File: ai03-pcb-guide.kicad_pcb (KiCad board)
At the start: 2 copper layers, 82.5 x 38.1 mm, 24 parts, among them SW1 SW_Push, U1 ATmega32U4-A, Y1 16Mhz

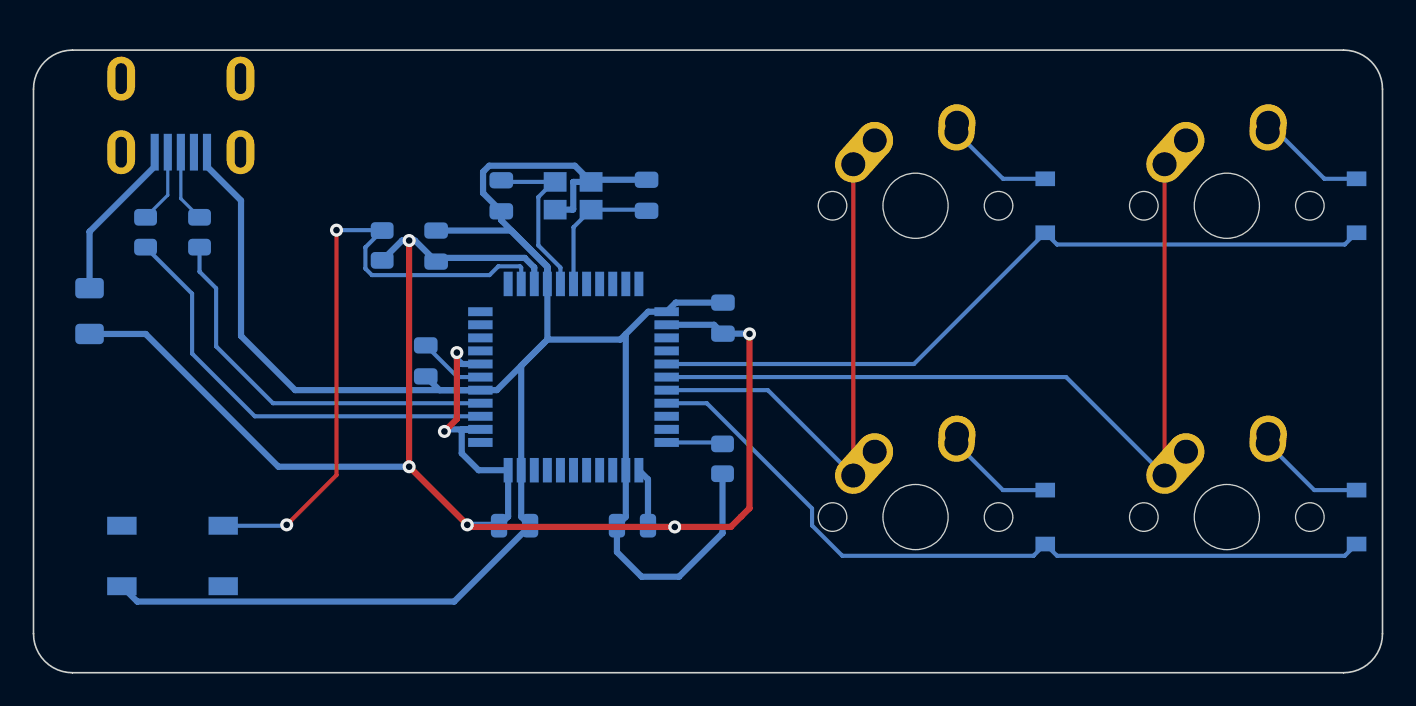
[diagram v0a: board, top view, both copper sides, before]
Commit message: Reroute PCB and add ground fill.
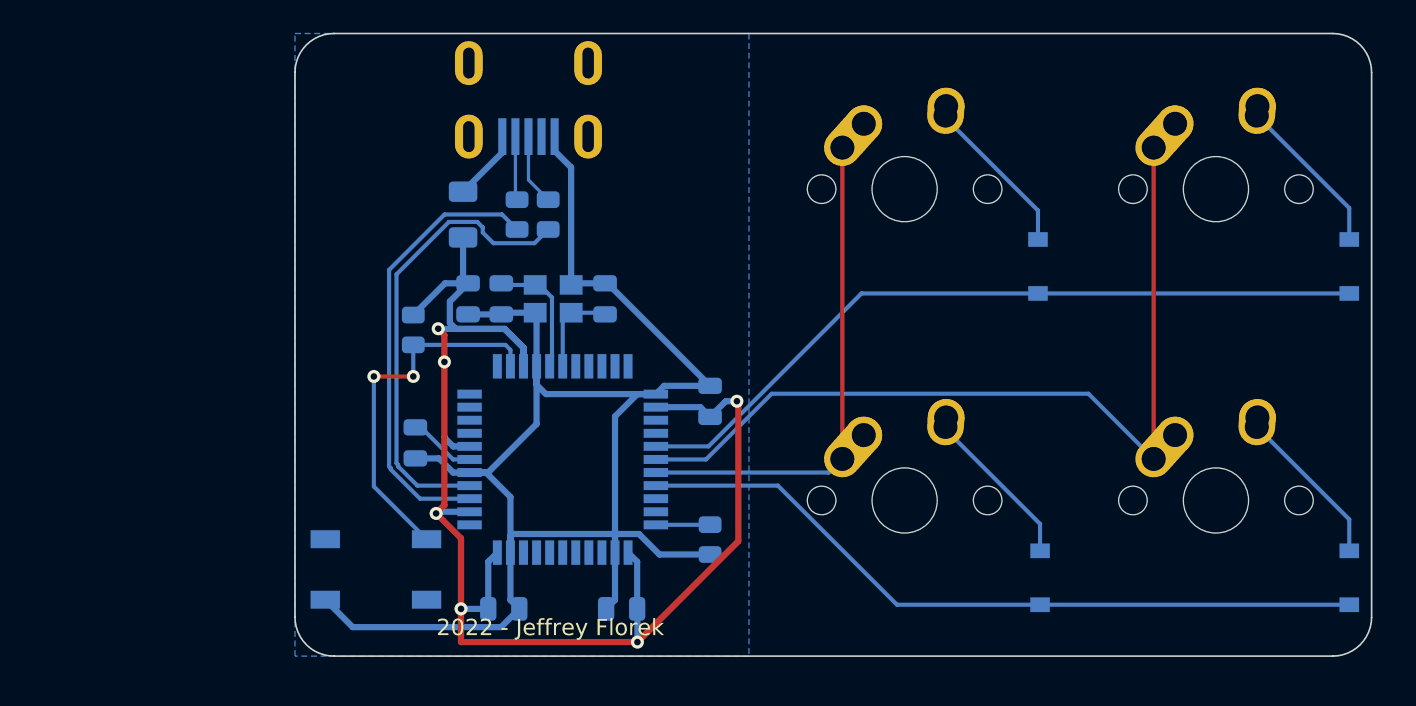
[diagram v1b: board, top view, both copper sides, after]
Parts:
- moved F1 23.6 mm to (118.2, 99.2)
- moved R3 22.8 mm to (121.5, 99.2)
- moved R2 21.4 mm to (123.4, 99.2)
- moved USB1 21.3 mm to (122.2, 89.9)
- moved SW1 12.5 mm to (112.9, 120.9)
- moved C1 6.83 mm to (126.9, 104.3)
- moved Y1 6.42 mm to (123.7, 104.3)
- moved C2 6.31 mm to (120.6, 104.3)
- moved R1 5.51 mm to (115.2, 106.2), turned to -90 degrees
- moved C5 5.15 mm to (133.3, 110.6)
- moved C6 5.14 mm to (127.9, 123.3)
- moved C7 5.14 mm to (120.7, 123.3)
- moved U1 5.08 mm to (124.3, 114.2)
- moved C3 5.06 mm to (115.3, 113.2)
- moved R4 5.00 mm to (133.3, 119.1)
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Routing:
- net GND: track 148.7 -> 106.1 mm
- net Net-(R1-Pad2): track 39.7 -> 22.7 mm
- net +5V: track 113.4 -> 96.5 mm, vias 7 -> 6
- net VCC: track 9.98 -> 4.37 mm
- net Net-(R2-Pad1): track 24.1 -> 28.3 mm
- net Net-(D3-Pad2): track 6.62 -> 9.98 mm
- net Net-(D1-Pad2): track 6.62 -> 9.93 mm
- net Net-(D4-Pad2): track 6.62 -> 9.93 mm
- net Net-(D2-Pad2): track 6.82 -> 9.93 mm
- net Net-(C2-Pad2): track 10.6 -> 7.73 mm
- net Net-(C1-Pad2): track 8.41 -> 5.61 mm
- net ROW1: track 47.6 -> 45.5 mm
- net COL0: track 32.6 -> 30.8 mm
- net COL1: track 52.0 -> 52.8 mm
- net D-: track 4.55 -> 3.90 mm
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- added copper zone on B.Cu, net GND
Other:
- board size 82.5 x 38.1 mm -> 65.9 x 38.1 mm
- board text added: "2022 - Jeffrey Florek"

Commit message: Add silly line art of my dog to the PCB.
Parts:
- added G***: LOGO, LOGO, F.Cu at (124.7, 107.6)
